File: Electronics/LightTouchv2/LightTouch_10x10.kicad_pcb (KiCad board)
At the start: 2 copper layers, 100 x 100 mm, 500 parts, among them Q1 RPM-075PTT86, Q10 SQJA26EP-T1_GE3, Q100 SQJA26EP-T1_GE3, Q101 RPM-075PTT86, Q102 SQJA26EP-T1_GE3, Q103 RPM-075PTT86, Q104 SQJA26EP-T1_GE3, Q105 RPM-075PTT86, Q106 SQJA26EP-T1_GE3, Q107 RPM-075PTT86, Q108 SQJA26EP-T1_GE3, Q109 RPM-075PTT86, Q11 RPM-075PTT86, Q110 SQJA26EP-T1_GE3, Q111 RPM-075PTT86, Q112 SQJA26EP-T1_GE3, Q113 RPM-075PTT86, Q114 SQJA26EP-T1_GE3, Q115 RPM-075PTT86, Q116 SQJA26EP-T1_GE3, Q117 RPM-075PTT86, Q118 SQJA26EP-T1_GE3, Q119 RPM-075PTT86, Q12 SQJA26EP-T1_GE3, Q120 SQJA26EP-T1_GE3, Q121 RPM-075PTT86, Q122 SQJA26EP-T1_GE3, Q123 RPM-075PTT86, Q124 SQJA26EP-T1_GE3, Q125 RPM-075PTT86, Q126 SQJA26EP-T1_GE3, Q127 RPM-075PTT86, Q128 SQJA26EP-T1_GE3, Q129 RPM-075PTT86, Q13 RPM-075PTT86, Q130 SQJA26EP-T1_GE3, Q131 RPM-075PTT86, Q132 SQJA26EP-T1_GE3, Q133 RPM-075PTT86, Q134 SQJA26EP-T1_GE3, Q135 RPM-075PTT86, Q136 SQJA26EP-T1_GE3, Q137 RPM-075PTT86, Q138 SQJA26EP-T1_GE3, Q139 RPM-075PTT86, Q14 SQJA26EP-T1_GE3, Q140 SQJA26EP-T1_GE3, Q141 RPM-075PTT86, Q142 SQJA26EP-T1_GE3, Q143 RPM-075PTT86, Q144 SQJA26EP-T1_GE3, Q145 RPM-075PTT86, Q146 SQJA26EP-T1_GE3, Q147 RPM-075PTT86, Q148 SQJA26EP-T1_GE3, Q149 RPM-075PTT86, Q15 RPM-075PTT86, Q150 SQJA26EP-T1_GE3, Q151 RPM-075PTT86, Q152 SQJA26EP-T1_GE3, Q153 RPM-075PTT86, Q154 SQJA26EP-T1_GE3, Q155 RPM-075PTT86, Q156 SQJA26EP-T1_GE3, Q157 RPM-075PTT86, Q158 SQJA26EP-T1_GE3, Q159 RPM-075PTT86, Q16 SQJA26EP-T1_GE3, Q160 SQJA26EP-T1_GE3, Q161 RPM-075PTT86, Q162 SQJA26EP-T1_GE3, Q163 RPM-075PTT86, Q164 SQJA26EP-T1_GE3, Q165 RPM-075PTT86, Q166 SQJA26EP-T1_GE3, Q167 RPM-075PTT86, Q168 SQJA26EP-T1_GE3, Q169 RPM-075PTT86, Q17 RPM-075PTT86, Q170 SQJA26EP-T1_GE3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

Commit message: PCB design with new MOSFETs
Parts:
- moved L56 11.4 mm to (84.3, 58.5)
- moved Q111 11.4 mm to (82.5, 60.0)
- moved Q112 11.4 mm to (86.8, 57.9)
- moved R156 11.4 mm to (82.8, 54.1)
- moved R56 11.4 mm to (82.8, 57.0)
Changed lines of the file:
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@@
 	(footprint "footprints:RC0402N_YAG"
 		(layer "F.Cu")
-		(at 93 59.0588 -90)
+		(at 82.75 54.0588 -90)
 		(tags "RC0402FR-07470RL ")
 		(property "Reference" "R156"
@@
 			(polygon
 				(pts
-					(xy 93.2032 58.881) (xy 93.2032 59.2366) (xy 92.7968 59.2366) (xy 92.7968 58.881)
+					(xy 82.9532 53.881) (xy 82.9532 54.2366) (xy 82.5468 54.2366) (xy 82.5468 53.881)
 				)
 			)
@@
 	(footprint "footprints:PowerPAK_SO-8L_3_VIS"
 		(layer "F.Cu")
-		(at 97 62.8697 180)
+		(at 86.75 57.8697 180)
 		(tags "SQJA26EP-T1_GE3 ")
 		(property "Reference" "Q112"
@@
 	(footprint "footprints:TRANS_RPM-075P_ROM"
 		(layer "F.Cu")
-		(at 92.75 65 -90)
+		(at 82.5 60 -90)
 		(tags "RPM-075PTT86 ")
 		(property "Reference" "Q111"
@@
 			(polygon
 				(pts
-					(xy 93.3215 64.3523) (xy 93.3215 65.6477) (xy 92.1785 65.6477) (xy 92.1785 64.3523)
+					(xy 83.0715 59.3523) (xy 83.0715 60.6477) (xy 81.9285 60.6477) (xy 81.9285 59.3523)
 				)
 			)
@@
 	(footprint "footprints:RES_CRCW0402_VIS"
 		(layer "F.Cu")
-		(at 93 61.9699 -90)
+		(at 82.75 56.9699 -90)
 		(tags "CRCW040250K0FKED ")
 		(property "Reference" "R56"
@@
 			(polygon
 				(pts
-					(xy 93.2286 61.8302) (xy 93.2286 62.1096) (xy 92.7714 62.1096) (xy 92.7714 61.8302)
+					(xy 82.9786 56.8302) (xy 82.9786 57.1096) (xy 82.5214 57.1096) (xy 82.5214 56.8302)
 				)
 			)
@@
 	(footprint "footprints:IND_BOURNS_SDR0604"
 		(layer "B.Cu")
-		(at 94.5696 63.5 180)
+		(at 84.3196 58.5 180)
 		(tags "SDR0604- 821KL ")
 		(property "Reference" "L56"
@@
 	)
 	(segment
-		(start 96.5 63.5)
-		(end 96.5 67)
+		(start 86.25 58.5)
+		(end 86.25 62)
 		(width 1.5)
 		(layer "B.Cu")
@@
 	)
 	(segment
-		(start 96.5 63.5)
-		(end 96.5 57)
+		(start 86.25 58.5)
+		(end 86.25 52)
 		(width 1.5)
 		(layer "B.Cu")
@@
 	)
 	(segment
-		(start 91.75 65.75)
-		(end 91.75 67)
+		(start 81.5 60.75)
+		(end 81.5 62)
 		(width 0.2)
 		(layer "F.Cu")
@@
 	)
 	(segment
-		(start 92.75 65.8509)
-		(end 91.8509 65.8509)
+		(start 82.5 60.8509)
+		(end 81.6009 60.8509)
 		(width 0.2)
 		(layer "F.Cu")
@@
 	)
 	(segment
-		(start 91.8509 65.8509)
-		(end 91.75 65.75)
+		(start 81.6009 60.8509)
+		(end 81.5 60.75)
 		(width 0.2)
 		(layer "F.Cu")
@@
 	)
 	(segment
-		(start 91.75 65.75)
-		(end 91.75 57)
+		(start 81.5 60.75)
+		(end 81.5 52)
 		(width 0.2)
 		(layer "F.Cu")
@@
 	)
 	(segment
-		(start 100.25 59.25)
-		(end 100.25 67)
+		(start 90 54.25)
+		(end 90 62)
 		(width 1.5)
 		(layer "F.Cu")
@@
 	)
 	(segment
-		(start 98.905 59.2629)
-		(end 100.2371 59.2629)
+		(start 88.655 54.2629)
+		(end 89.9871 54.2629)
 		(width 1.5)
 		(layer "F.Cu")
@@
 	)
 	(segment
-		(start 94.9699 60.726)
-		(end 98 60.726)
+		(start 84.7199 55.726)
+		(end 87.75 55.726)
 		(width 0.2)
 		(layer "F.Cu")
@@
 	)
 	(segment
-		(start 98.905 59.821)
-		(end 98.905 59.2629)
+		(start 88.655 54.821)
+		(end 88.655 54.2629)
 		(width 0.2)
 		(layer "F.Cu")
@@
 	)
 	(segment
-		(start 98 60.726)
-		(end 98.905 59.821)
+		(start 87.75 55.726)
+		(end 88.655 54.821)
 		(width 0.2)
 		(layer "F.Cu")
@@
 	)
 	(segment
-		(start 100.2371 59.2629)
-		(end 100.25 59.25)
+		(start 89.9871 54.2629)
+		(end 90 54.25)
 		(width 0.2)
 		(layer "F.Cu")
@@
 	)
 	(segment
-		(start 93.2561 62.4398)
-		(end 93 62.4398)
+		(start 83.0061 57.4398)
+		(end 82.75 57.4398)
 		(width 0.2)
 		(layer "F.Cu")
@@
 	)
 	(segment
-		(start 100.25 59.25)
-		(end 100.25 57)
+		(start 90 54.25)
+		(end 90 52)
 		(width 1.5)
 		(layer "F.Cu")
@@
 	)
 	(segment
-		(start 94.9699 60.726)
-		(end 93.2561 62.4398)
+		(start 84.7199 55.726)
+		(end 83.0061 57.4398)
 		(width 0.2)
 		(layer "F.Cu")
@@
 	)
 	(segment
-		(start 95.865831 65.134169)
-		(end 94.399527 65.134169)
+		(start 85.615831 60.134169)
+		(end 84.149527 60.134169)
 		(width 1.5)
 		(layer "F.Cu")
@@
 	)
 	(segment
-		(start 97 64)
-		(end 95.865831 65.134169)
+		(start 86.75 59)
+		(end 85.615831 60.134169)
 		(width 1.5)
 		(layer "F.Cu")
@@
 	)
 	(via
-		(at 94.399527 65.134169)
+		(at 84.149527 60.134169)
 		(size 1.5)
 		(drill 0.8)
@@
 	)
 	(segment
-		(start 94.399527 65.134169)
-		(end 94.273369 65.134169)
+		(start 84.149527 60.134169)
+		(end 84.023369 60.134169)
 		(width 1.5)
 		(layer "B.Cu")
@@
 	)
 	(segment
-		(start 94.273369 65.134169)
-		(end 92.6392 63.5)
+		(start 84.023369 60.134169)
+		(end 82.3892 58.5)
 		(width 1.5)
 		(layer "B.Cu")
@@
 	)
 	(segment
-		(start 93 61.5)
-		(end 93 59.6176)
+		(start 82.75 56.5)
+		(end 82.75 54.6176)
 		(width 0.2)
 		(layer "F.Cu")
@@
 	)
 	(segment
-		(start 92.25 63.6491)
-		(end 92.25 60.3676)
+		(start 82 58.6491)
+		(end 82 55.3676)
 		(width 0.2)
 		(layer "F.Cu")
@@
 	)
 	(segment
-		(start 92.25 60.3676)
-		(end 93 59.6176)
+		(start 82 55.3676)
+		(end 82.75 54.6176)
 		(width 0.2)
 		(layer "F.Cu")
@@
 	)
 	(segment
-		(start 92.75 64.1491)
-		(end 92.25 63.6491)
+		(start 82.5 59.1491)
+		(end 82 58.6491)
 		(width 0.2)
 		(layer "F.Cu")
@@
 	)
 	(segment
-		(start 93 58.5)
-		(end 94.3321 58.5)
+		(start 82.75 53.5)
+		(end 84.0821 53.5)
 		(width 0.2)
 		(layer "F.Cu")
@@
 	)
 	(segment
-		(start 94.3321 58.5)
-		(end 95.095 59.2629)
+		(start 84.0821 53.5)
+		(end 84.845 54.2629)
 		(width 0.2)
 		(layer "F.Cu")

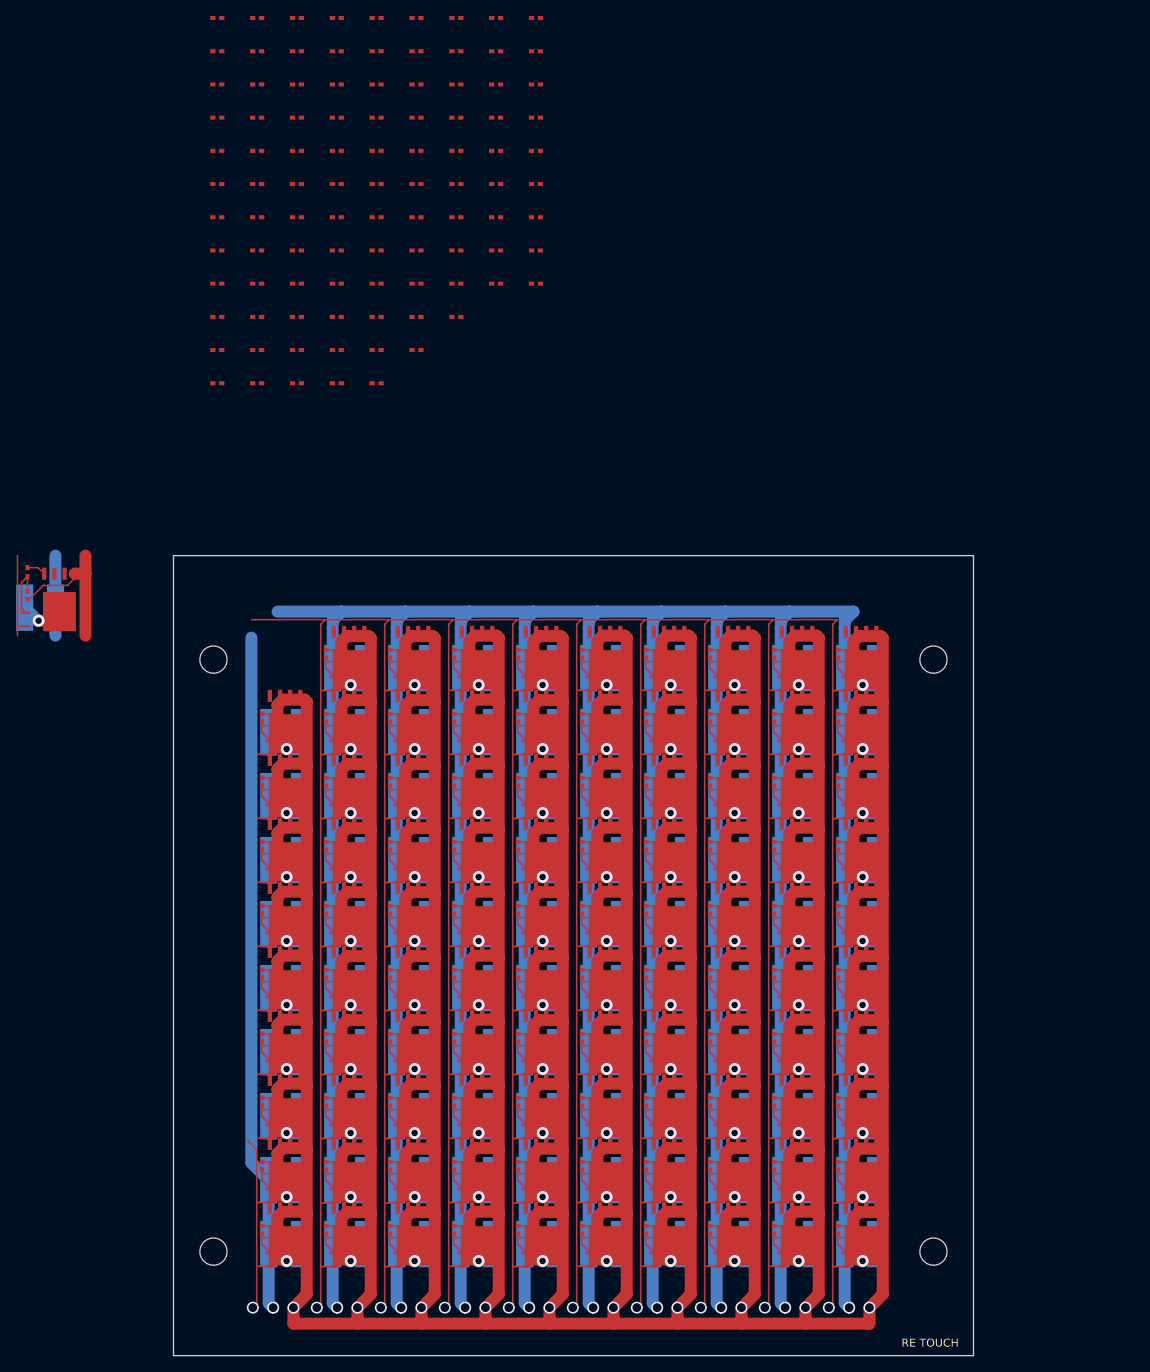
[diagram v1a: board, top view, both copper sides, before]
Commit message: Finished 10x10 PCB with new mosfets
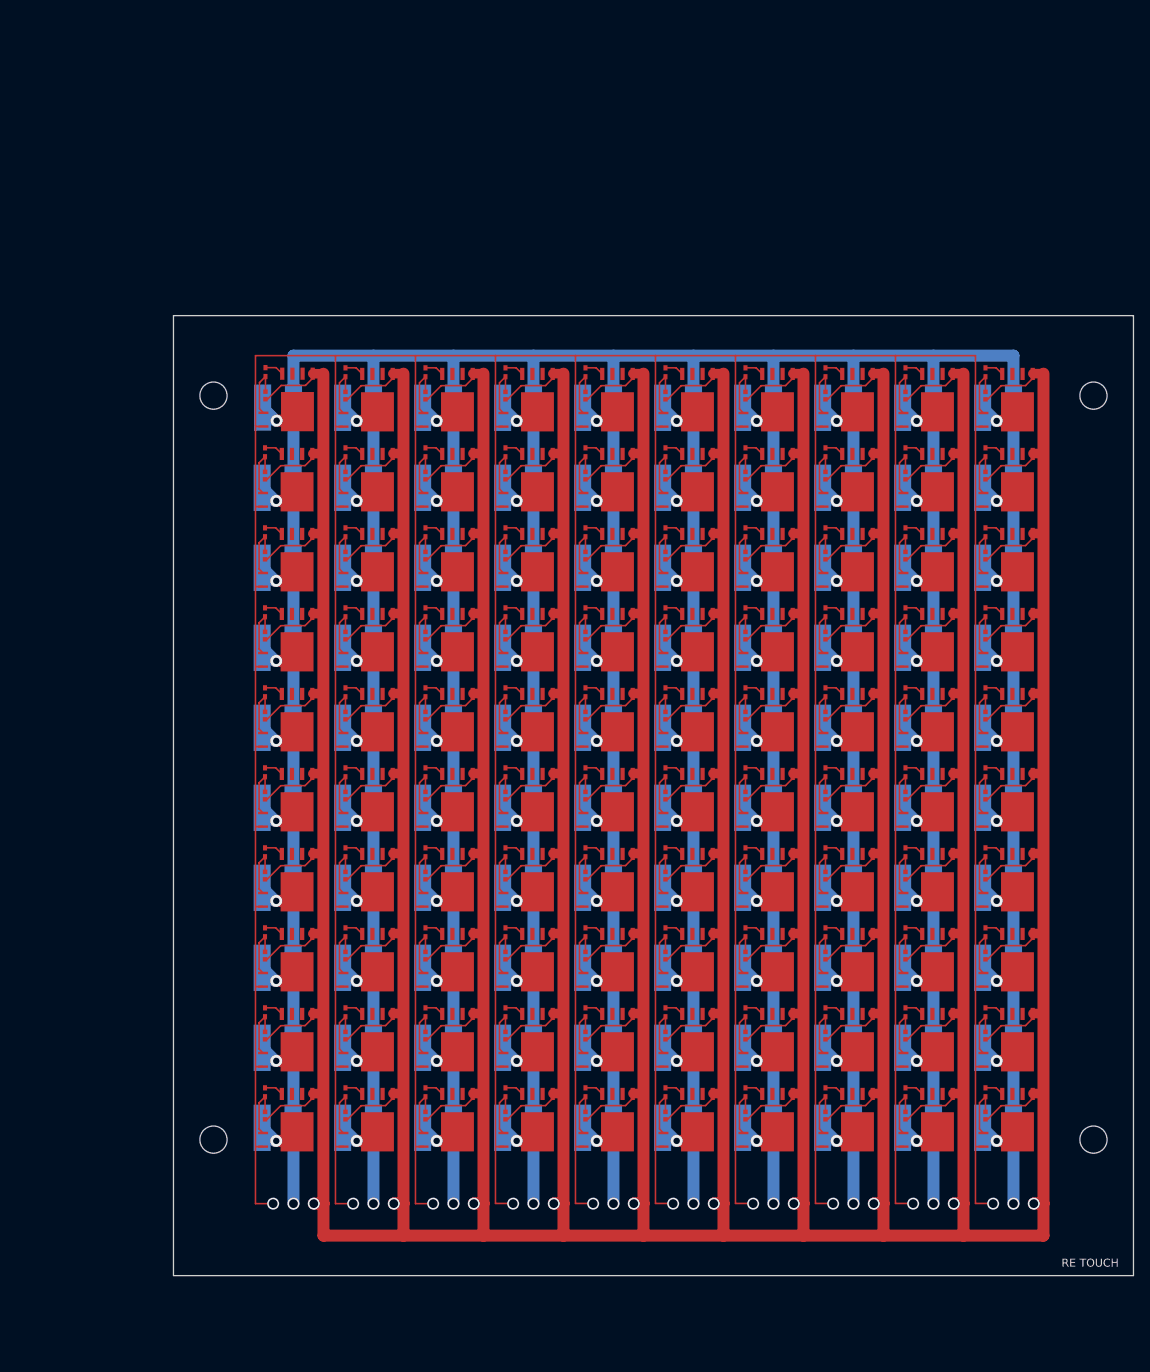
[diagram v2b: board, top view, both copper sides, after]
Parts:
- moved R180 136.4 mm to (202.5, 119.1), turned to -90 degrees
- moved R103 134.4 mm to (112.5, 119.1), turned to -90 degrees
- moved R158 132.7 mm to (192.5, 119.1), turned to -90 degrees
- moved R149 131.1 mm to (122.5, 119.1), turned to -90 degrees
- moved R127 129.8 mm to (182.5, 119.1), turned to -90 degrees
- moved R199 128.6 mm to (132.5, 119.1), turned to -90 degrees
- moved R153 127.8 mm to (172.5, 119.1), turned to -90 degrees
- moved R183 127.0 mm to (142.5, 119.1), turned to -90 degrees
- moved R150 126.6 mm to (162.5, 119.1), turned to -90 degrees
- moved R193 126.4 mm to (152.5, 119.1), turned to -90 degrees
- moved R137 125.9 mm to (202.5, 109.1), turned to -90 degrees
- moved R101 124.3 mm to (112.5, 109.1), turned to -90 degrees
- moved R164 121.9 mm to (192.5, 109.1), turned to -90 degrees
- moved R190 120.6 mm to (122.5, 109.1), turned to -90 degrees
- moved R151 118.8 mm to (182.5, 109.1), turned to -90 degrees
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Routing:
- net GND: track 1706.6 -> 2067.7 mm
- net +10V: track 1046.4 -> 1262.1 mm
- net +20V: track 956.0 -> 1150.0 mm
- net Net-(Q99-E): track 0.00 -> 6.93 mm
- net Net-(Q9-E): track 0.00 -> 6.93 mm
- net Net-(Q100-G): track 7.24 -> 2.41 mm
- net Net-(Q10-G): track 7.24 -> 2.41 mm
- net Net-(Q94-G): track 0.00 -> 2.41 mm
- net Net-(Q88-G): track 0.00 -> 2.41 mm
- net Net-(Q84-G): track 0.00 -> 2.41 mm
- net Net-(Q80-G): track 0.00 -> 2.41 mm
- net Net-(Q8-G): track 0.00 -> 2.41 mm
- net Net-(Q70-G): track 0.00 -> 2.41 mm
- net Net-(Q62-G): track 0.00 -> 2.41 mm
- net Net-(Q58-G): track 0.00 -> 2.41 mm
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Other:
- board size 100 x 100 mm -> 120 x 120 mm
